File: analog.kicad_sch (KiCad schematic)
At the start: 38 parts, among them IC10 DAC5571IDBVR, IC6 MCP6S91-E_MS, IC7 MCP6S91-E_MS, IC8 MCP4726A0T-E_CH, IC9 DAC5571IDBVR, K1 AQY210EHAX, K2 AQY210EHAX, U10 MCP6022T-I_SN, U8 MCP6022T-I_SN, U9 MCP6022T-I_SN

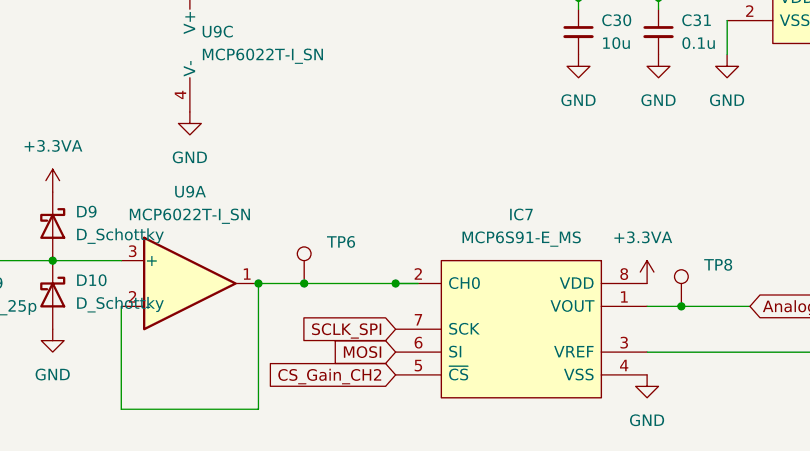
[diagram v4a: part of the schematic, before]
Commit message: changed adc and esp chip
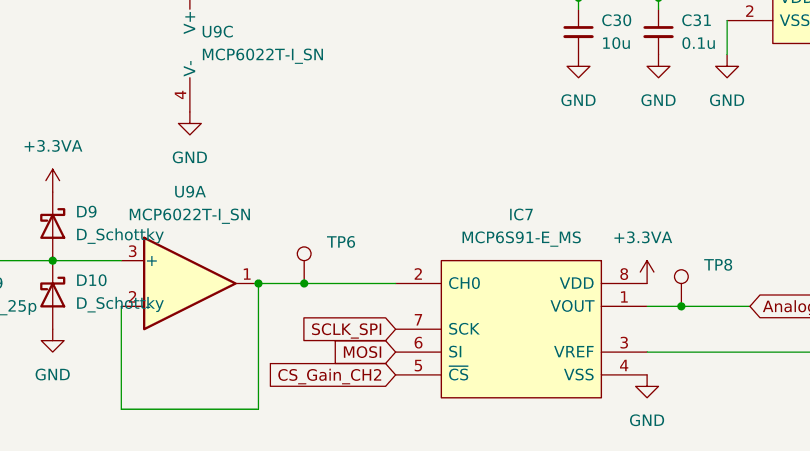
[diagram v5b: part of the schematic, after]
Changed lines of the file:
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@@
   (junction (at 144.78 113.03) (diameter 0) (color 0 0 0 0)
-  )
-  (junction (at 115.57 144.78) (diameter 0) (color 0 0 0 0)
   )
   (junction (at 55.88 142.24) (diameter 0) (color 0 0 0 0)
@@
     (stroke (width 0) (type default) (color 0 0 0 0))
   )
-  (wire (pts (xy 118.11 144.78) (xy 115.57 144.78))
-    (stroke (width 0) (type default) (color 0 0 0 0))
-  )

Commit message: updated circuit
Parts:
- removed IC10, IC9: DAC5571IDBVR, project_library:DAC5571IDBVR, symbol project_library:DAC5571IDBVR
- J3, J4: footprint 73100-0105 -> project_library:73100-0105
- TP10: value ? -> OFFCH2
- TP11: value ? -> TRIGREF
- TP5: value ~ -> ANICH1
- TP6: value ~ -> ANICH2
- TP7: value ~ -> ANOCH1
- TP8: value ~ -> ANOCH2
- TP9: value ? -> OFFCH1

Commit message: routing
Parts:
- C30: value 10u -> (none); footprint Capacitor_SMD:C_0805_2012Metric_Pad1.18x1.45mm_HandSolder -> (none)
- C31, C32: value 0.1u -> (none); footprint Capacitor_SMD:C_0805_2012Metric_Pad1.18x1.45mm_HandSolder -> (none)
- R22, R23: value 835k -> (none)
- R24, R25: value 165k -> (none)
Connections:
- net GND is gone; now on net GNDA: C30.2, C31.2, C32.2, D10.2 (A), D8.2 (A), IC6.4 (VSS), IC7.4 (VSS), IC8.2 (VSS), U10.4 (V-), U8.4 (V-), U9.4 (V-)
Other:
- moved on the sheet: U10C

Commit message: routing
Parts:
- C30: value (none) -> 10u; footprint (none) -> Capacitor_SMD:C_0603_1608Metric_Pad1.08x0.95mm_HandSolder
- C31, C32: value (none) -> 0.1u; footprint (none) -> Capacitor_SMD:C_0603_1608Metric_Pad1.08x0.95mm_HandSolder
- R22, R23: value (none) -> 900k
- R24, R25: value (none) -> 100k
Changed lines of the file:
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@@
       (effects (font (size 1.27 1.27)) (justify left))
     )
-    (property "Value" "" (id 1) (at 62.23 147.32 0)
+    (property "Value" "100k" (id 1) (at 62.23 147.32 0)
       (effects (font (size 1.27 1.27)) (justify left))
     )
@@
       (effects (font (size 1.27 1.27)) (justify left))
     )
-    (property "Value" "" (id 1) (at 138.43 118.1162 0)
-      (effects (font (size 1.27 1.27)) (justify left))
-    )
-    (property "Footprint" "" (id 2) (at 135.89 116.84 0)
+    (property "Value" "10u" (id 1) (at 138.43 118.1162 0)
+      (effects (font (size 1.27 1.27)) (justify left))
+    )
+    (property "Footprint" "Capacitor_SMD:C_0603_1608Metric_Pad1.08x0.95mm_HandSolder" (id 2) (at 135.89 116.84 0)
       (effects (font (size 1.27 1.27)) hide)
     )
@@
     (in_bom yes) (on_board yes) (fields_autoplaced)
     (property "Reference" "R23" (id 0) (at 46.99 135.89 90))
-    (property "Value" "" (id 1) (at 46.99 138.43 90))
+    (property "Value" "900k" (id 1) (at 46.99 138.43 90))
     (property "Footprint" "Resistor_SMD:R_0805_2012Metric_Pad1.20x1.40mm_HandSolder" (id 2) (at 46.99 142.24 0)
       (effects (font (size 1.27 1.27)) hide)
@@
       (effects (font (size 1.27 1.27)) (justify left))
     )
-    (property "Value" "" (id 1) (at 185.42 118.1162 0)
-      (effects (font (size 1.27 1.27)) (justify left))
-    )
-    (property "Footprint" "" (id 2) (at 182.88 116.84 0)
+    (property "Value" "0.1u" (id 1) (at 185.42 118.1162 0)
+      (effects (font (size 1.27 1.27)) (justify left))
+    )
+    (property "Footprint" "Capacitor_SMD:C_0603_1608Metric_Pad1.08x0.95mm_HandSolder" (id 2) (at 182.88 116.84 0)
       (effects (font (size 1.27 1.27)) hide)
     )
@@
     (in_bom yes) (on_board yes) (fields_autoplaced)
     (property "Reference" "R22" (id 0) (at 44.45 59.69 90))
-    (property "Value" "" (id 1) (at 44.45 62.23 90))
+    (property "Value" "900k" (id 1) (at 44.45 62.23 90))
     (property "Footprint" "Resistor_SMD:R_0805_2012Metric_Pad1.20x1.40mm_HandSolder" (id 2) (at 44.45 66.04 0)
       (effects (font (size 1.27 1.27)) hide)
@@
       (effects (font (size 1.27 1.27)) (justify left))
     )
-    (property "Value" "" (id 1) (at 147.32 118.1162 0)
-      (effects (font (size 1.27 1.27)) (justify left))
-    )
-    (property "Footprint" "" (id 2) (at 144.78 116.84 0)
+    (property "Value" "0.1u" (id 1) (at 147.32 118.1162 0)
+      (effects (font (size 1.27 1.27)) (justify left))
+    )
+    (property "Footprint" "Capacitor_SMD:C_0603_1608Metric_Pad1.08x0.95mm_HandSolder" (id 2) (at 144.78 116.84 0)
       (effects (font (size 1.27 1.27)) hide)
     )
@@
       (effects (font (size 1.27 1.27)) (justify left))
     )
-    (property "Value" "" (id 1) (at 59.69 71.12 0)
-      (effects (font (size 1.27 1.27)) (justify left))
-    )
+    (property "Value" "100k" (id 1) (at 59.69 71.12 0)
+      (effects (font (size 1.27 1.27)) (justify left))
+    )
